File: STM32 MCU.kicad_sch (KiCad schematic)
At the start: 21 parts, among them SW3 SW_Push, SW4 SW_Push, U2 STM32G474RETx, Y1 Crystal

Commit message: Small changes
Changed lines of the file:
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@@
-		)
-	)
-	(label "FAN_PWM"
-		(at 177.8 44.45 0)
-		(effects
-			(font
-				(size 1.27 1.27)
-			)
-			(justify left bottom)
 		)
 	)
@@
 		)
 	)
+	(hierarchical_label "FAN_PWM"
+		(shape input)
+		(at 177.8 44.45 0)
+		(effects
+			(font
+				(size 1.27 1.27)
+			)
+			(justify left)
+		)
+	)

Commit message: added RTC
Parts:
- added BT1: Battery_Cell, Battery:BatteryHolder_Keystone_3000_1x12mm, symbol Device:Battery_Cell
- added U4: RV-3028-C7, Package_SON:MicroCrystal_C7_SON-8_1.5x3.2mm_P0.9mm, symbol Timer_RTC:RV-3028-C7
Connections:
- net +3V3: now also U4.7 (VDD)
- net GND: now also BT1.2 (-), U4.5 (VSS), U4.8 (EVI)
- net I2C3_SCL: now also U4.3 (SCL)
- net I2C3_SDA: now also U4.4 (SDA)
- net INT_RTC: now reaches U2.38 (PC6)
- net INT_RTC: now also U4.2 (~{INT})
- new net: BT1.1 (+), U4.6 (VBACKUP)
- no-connect marks 0 -> 1
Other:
- note added: "REAL TIME CLOCK"

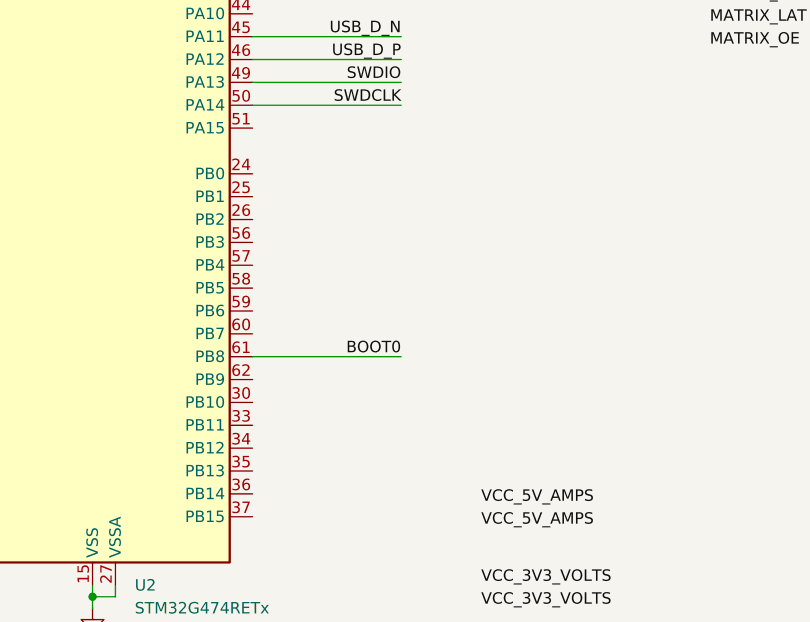
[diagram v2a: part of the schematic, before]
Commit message: added charge pump, fixed analog audio
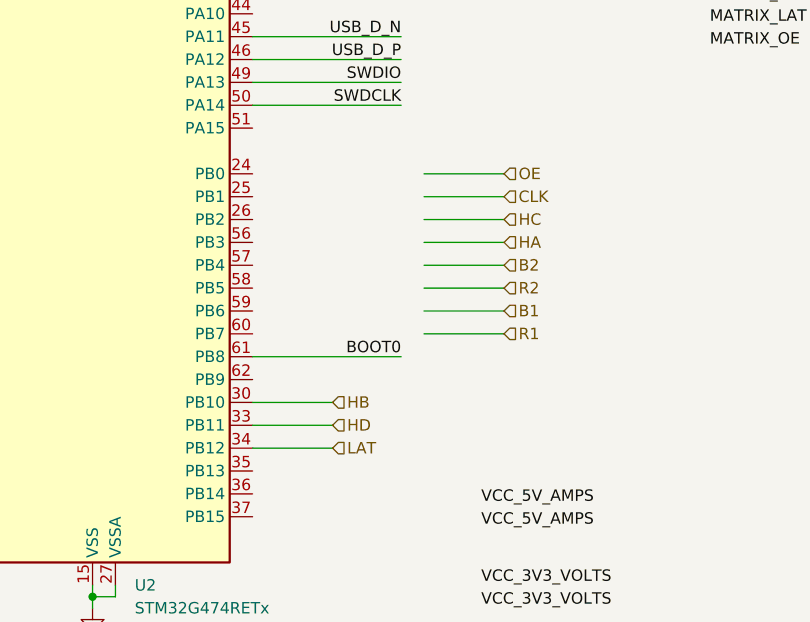
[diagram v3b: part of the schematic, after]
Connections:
- net HB: now reaches U2.30 (PB10)
- net HD: now reaches U2.33 (PB11)
- net LAT: now reaches U2.34 (PB12)
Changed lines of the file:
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@@
+	(wire
+		(pts
+			(xy 180.34 97.79) (xy 171.45 97.79)
+		)
+		(stroke
+			(width 0)
+			(type default)
+		)
+	)
 	(wire
 		(pts
@@
 	(wire
 		(pts
+			(xy 152.4 115.57) (xy 161.29 115.57)
+		)
+		(stroke
+			(width 0)
+			(type default)
+		)
+	)
+	(wire
+		(pts
 			(xy 104.14 25.4) (xy 99.06 25.4)
 		)
@@
 	(wire
 		(pts
+			(xy 152.4 120.65) (xy 161.29 120.65)
+		)
+		(stroke
+			(width 0)
+			(type default)
+		)
+	)
+	(wire
+		(pts
 			(xy 243.84 76.2) (xy 243.84 80.01)
 		)
@@
 	(wire
 		(pts
+			(xy 180.34 95.25) (xy 171.45 95.25)
+		)
+		(stroke
+			(width 0)
+			(type default)
+		)
+	)
+	(wire
+		(pts
 			(xy 152.4 110.49) (xy 168.91 110.49)
 		)
@@
 	(wire
 		(pts
+			(xy 152.4 118.11) (xy 161.29 118.11)
+		)
+		(stroke
+			(width 0)
+			(type default)
+		)
+	)
+	(wire
+		(pts
 			(xy 48.26 162.56) (xy 48.26 163.83)
 		)
@@
 	(wire
 		(pts
+			(xy 180.34 90.17) (xy 171.45 90.17)
+		)
+		(stroke
+			(width 0)
+			(type default)
+		)
+	)
+	(wire
+		(pts
 			(xy 93.98 35.56) (xy 88.9 35.56)
 		)
@@
 	(wire
 		(pts
+			(xy 180.34 100.33) (xy 171.45 100.33)
+		)
+		(stroke
+			(width 0)
+			(type default)
+		)
+	)
+	(wire
+		(pts
 			(xy 243.84 72.39) (xy 243.84 76.2)
 		)
@@
 	(wire
 		(pts
+			(xy 180.34 102.87) (xy 171.45 102.87)
+		)
+		(stroke
+			(width 0)
+			(type default)
+		)
+	)
+	(wire
+		(pts
 			(xy 260.35 115.57) (xy 264.16 115.57)
 		)
@@
 	(wire
 		(pts
+			(xy 180.34 92.71) (xy 171.45 92.71)
+		)
+		(stroke
+			(width 0)
+			(type default)
+		)
+	)
+	(wire
+		(pts
 			(xy 93.98 34.29) (xy 93.98 35.56)
 		)
@@
 	(wire
 		(pts
+			(xy 180.34 107.95) (xy 171.45 107.95)
+		)
+		(stroke
+			(width 0)
+			(type default)
+		)
+	)
+	(wire
+		(pts
 			(xy 116.84 100.33) (xy 99.06 100.33)
 		)
@@
 		(pts
 			(xy 152.4 54.61) (xy 166.37 54.61)
+		)
+		(stroke
+			(width 0)
+			(type default)
+		)
+	)
+	(wire
+		(pts
+			(xy 180.34 105.41) (xy 171.45 105.41)
 		)
 		(stroke
@@
 		)
 	)
+	(hierarchical_label "R2"
+		(shape input)
+		(at 180.34 102.87 0)
+		(effects
+			(font
+				(size 1.27 1.27)
+			)
+			(justify left)
+		)
+	)
 	(hierarchical_label "PC_7"
 		(shape input)
@@
 		)
 	)
+	(hierarchical_label "B2"
+		(shape input)
+		(at 180.34 100.33 0)
+		(effects
+			(font
+				(size 1.27 1.27)
+			)
+			(justify left)
+		)
+	)
 	(hierarchical_label "I2S3_WS"
 		(shape input)
@@
 		)
 	)
+	(hierarchical_label "OE"
+		(shape input)
+		(at 180.34 90.17 0)
+		(effects
+			(font
+				(size 1.27 1.27)
+			)
+			(justify left)
+		)
+	)
 	(hierarchical_label "ADC1_IN3"
 		(shape input)
@@
 		)
 	)
+	(hierarchical_label "CLK"
+		(shape input)
+		(at 180.34 92.71 0)
+		(effects
+			(font
+				(size 1.27 1.27)
+			)
+			(justify left)
+		)
+	)
+	(hierarchical_label "LAT"
+		(shape input)
+		(at 161.29 120.65 0)
+		(effects
+			(font
+				(size 1.27 1.27)
+			)
+			(justify left)
+		)
+	)
 	(hierarchical_label "PC_11"
 		(shape input)
@@
 		)
 	)
+	(hierarchical_label "R1"
+		(shape input)
+		(at 180.34 107.95 0)
+		(effects
+			(font
+				(size 1.27 1.27)
+			)
+			(justify left)
+		)
+	)
+	(hierarchical_label "HB"
+		(shape input)
+		(at 161.29 115.57 0)
+		(effects
+			(font
+				(size 1.27 1.27)
+			)
+			(justify left)
+		)
+	)
 	(hierarchical_label "I2S3_SD"
 		(shape input)
@@
 		)
 	)
+	(hierarchical_label "HD"
+		(shape input)
+		(at 161.29 118.11 0)
+		(effects
+			(font
+				(size 1.27 1.27)
+			)
+			(justify left)
+		)
+	)
 	(hierarchical_label "I2C3_SDA"
 		(shape input)
@@
 		)
 	)
+	(hierarchical_label "HC"
+		(shape input)
+		(at 180.34 95.25 0)
+		(effects
+			(font
+				(size 1.27 1.27)
+			)
+			(justify left)
+		)
+	)
+	(hierarchical_label "B1"
+		(shape input)
+		(at 180.34 105.41 0)
+		(effects
+			(font
+				(size 1.27 1.27)
+			)
+			(justify left)
+		)
+	)
 	(hierarchical_label "FAN_PWM"
 		(shape input)
@@
 		(effects
 			(font
+				(size 1.27 1.27)
+			)
+			(justify left)
+		)
+	)
+	(hierarchical_label "HA"
+		(shape input)
+		(at 180.34 97.79 0)
+		(effects
+			(font

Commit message: added conenctors, barreljack
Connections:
- net B1: now also U2.25 (PB1)
- net B2: now also U2.23 (PC5)
- net CLK: now also U2.20 (PA6)
- net HA: now also U2.22 (PC4)
- net HC: now also U2.21 (PA7)
- net OE: now also U2.19 (PA5)
- net R1: now also U2.26 (PB2)
- net R2: now also U2.24 (PB0)

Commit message: Minor tweaks
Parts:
- added C37, C38: C, symbol Device:C
- added Y3: Crystal, Package_QFP:LQFP-64_10x10mm_P0.5mm, symbol Device:Crystal
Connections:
- net ADC1_IN3: no longer U2.14 (PA2)
- net GND: now also C37.2, C38.2
- net I2C3_SCL: no longer U2.40 (PC8), U4.3 (SCL)
- net I2C3_SDA: no longer U2.41 (PC9), U4.4 (SDA)
- net I2S3_CK: no longer U2.52 (PC10)
- net I2S3_SD: no longer U2.54 (PC12)
- net I2S3_WS: no longer U2.18 (PA4)
- net INT_RTC: no longer U2.38 (PC6)
- net MIC: no longer U2.8 (PC0)
- net PAPIR: no longer U2.9 (PC1)
- net PC_11: no longer U2.53 (PC11)
- net PC_7: no longer U2.39 (PC7)
- net RTC_CLK_IN: now also C37.1, Y3.2
- net RTC_CLK_OUT: now also C38.1, Y3.1
- net B1: no longer names the net of U2.25 (PB1)
- net B2: no longer names the net of U2.23 (PC5)
- net CLK: no longer names the net of U2.20 (PA6)
- net HA: no longer names the net of U2.22 (PC4)
- net HB: no longer names the net of U2.30 (PB10)
- net HC: no longer names the net of U2.21 (PA7)
- net HD: no longer names the net of U2.33 (PB11)
- net LAT: no longer names the net of U2.34 (PB12)
- net OE: no longer names the net of U2.19 (PA5)
- net PA_3: no longer names the net of U2.17 (PA3)
- net R1: no longer names the net of U2.26 (PB2)
- net R2: no longer names the net of U2.24 (PB0)
- new net I2C_SCL: U4.3 (SCL)
- new net I2C_SDA: U4.4 (SDA)
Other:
- note added: "CRYSTAL RTC"

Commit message: fixing power
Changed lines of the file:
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@@
+		)
+	)
+	(hierarchical_label "LED_On"
+		(shape input)
+		(at 85.09 130.81 180)
+		(effects
+			(font
+				(size 1.27 1.27)
+			)
+			(justify right)
 		)
 	)

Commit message: Wednesday minor changes
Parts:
- added D6, D9: LED, symbol Device:LED
- added R36, R48: 330, Package_DIP:DIP-8_W7.62mm, symbol Device:R
- added R46, R47: 5k1, Package_DIP:DIP-8_W7.62mm, symbol Device:R
- added R55: 10k, Package_DIP:DIP-8_W7.62mm, symbol Device:R
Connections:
- net I2C_SCL is gone; now on net I2C3_SCL: U4.3 (SCL)
- net I2C_SDA is gone; now on net I2C3_SDA: U4.4 (SDA)
- net +3V3: now also R36.1, R46.2, R47.2, R55.1
- net 5V_VOLTS: now also U2.17 (PA3)
- net ALS_ADC: now also U2.12 (PA0)
- net EXT_TEMP: now also U2.14 (PA2)
- net FAN_PWM: now also U2.9 (PC1)
- net GND: now also D6.1 (K), D9.1 (K)
- net I2C3_SCL: now also U2.42 (PA8), R46.1
- net I2C3_SDA: now also U2.41 (PC9), R47.1
- net MIC_ADC: now also U2.13 (PA1)
- net TV_IR_PWM: now also U2.8 (PC0)
- net at U2.18 (PA4): now also R55.2
- new net: D9.2 (A), R48.2
- new net: D6.2 (A), R36.2
- new net TEST_LED: R48.1
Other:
- note added: "I2C PULLUPS"
- note added: "TEST LED"
- moved on the sheet: C11, C3, C37, C38, R3, R4, Y1, Y3

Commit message: hooking stuff up to STM
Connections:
- net I2C3_SDA: now also U2.53 (PC11); no longer U2.41 (PC9)
- net I2S3_CK: now also U2.35 (PB13)
- net I2S3_SD: now also U2.37 (PB15)
- net I2S3_WS: now also U2.34 (PB12)
- net SPI_CS_ESP: now also U2.22 (PC4)
- net SPI_MISO: now also U2.20 (PA6)
- net SPI_MOSI: now also U2.21 (PA7)
- net SPI_SCLK: now also U2.19 (PA5)
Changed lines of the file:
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@@
 			(width 0)
 			(type default)
+			(color 0 194 194 1)
 		)
 	)
@@
 			(width 0)
 			(type default)
+			(color 0 194 194 1)
 		)
 	)
@@
 	(wire
 		(pts
+			(xy 185.42 119.38) (xy 189.23 119.38)
+		)
+		(stroke
+			(width 0)
+			(type default)
+			(color 0 0 194 1)
+		)
+	)
+	(wire
+		(pts
 			(xy 125.73 162.56) (xy 125.73 163.83)
 		)
@@
 	(wire
 		(pts
+			(xy 152.4 128.27) (xy 166.37 128.27)
+		)
+		(stroke
+			(width 0)
+			(type default)
+			(color 194 0 194 1)
+		)
+	)
+	(wire
+		(pts
 			(xy 40.64 93.98) (xy 40.64 96.52)
 		)
@@
 	(wire
 		(pts
+			(xy 152.4 123.19) (xy 166.37 123.19)
+		)
+		(stroke
+			(width 0)
+			(type default)
+			(color 194 0 194 1)
+		)
+	)
+	(wire
+		(pts
 			(xy 152.4 54.61) (xy 156.21 54.61)
 		)
@@
 	(wire
 		(pts
+			(xy 185.42 127) (xy 189.23 127)
+		)
+		(stroke
+			(width 0)
+			(type default)
+			(color 0 0 194 1)
+		)
+	)
+	(wire
+		(pts
 			(xy 80.01 25.4) (xy 80.01 26.67)
 		)
@@
 	(wire
 		(pts
+			(xy 152.4 64.77) (xy 177.8 64.77)
+		)
+		(stroke
+			(width 0)
+			(type default)
+			(color 221 133 0 1)
+		)
+	)
+	(wire
+		(pts
 			(xy 35.56 96.52) (xy 40.64 96.52)
 		)
@@
 	(wire
 		(pts
+			(xy 152.4 120.65) (xy 166.37 120.65)
+		)
+		(stroke
+			(width 0)
+			(type default)
+			(color 194 0 194 1)
+		)
+	)
+	(wire
+		(pts
 			(xy 243.84 76.2) (xy 243.84 80.01)
 		)
@@
 	(wire
 		(pts
+			(xy 185.42 124.46) (xy 189.23 124.46)
+		)
+		(stroke
+			(width 0)
+			(type default)
+			(color 0 0 194 1)
+		)
+	)
+	(wire
+		(pts
 			(xy 88.9 35.56) (xy 80.01 35.56)
 		)
@@
 	(wire
 		(pts
+			(xy 105.41 80.01) (xy 116.84 80.01)
+		)
+		(stroke
+			(width 0)
+			(type default)
+			(color 221 133 0 1)
+		)
+	)
+	(wire
+		(pts
 			(xy 85.09 171.45) (xy 85.09 180.34)
 		)
@@
 	(wire
 		(pts
+			(xy 185.42 121.92) (xy 189.23 121.92)
+		)
+		(stroke
+			(width 0)
+			(type default)
+			(color 0 0 194 1)
+		)
+	)
+	(wire
+		(pts
 			(xy 99.06 52.07) (xy 116.84 52.07)
 		)
@@
 	(wire
 		(pts
+			(xy 185.42 129.54) (xy 189.23 129.54)
+		)
+		(stroke
+			(width 0)
+			(type default)
+			(color 0 0 194 1)
+		)
+	)
+	(wire
+		(pts
 			(xy 134.62 137.16) (xy 137.16 137.16)
 		)
@@
 	(wire
 		(pts
+			(xy 109.22 97.79) (xy 116.84 97.79)
+		)
+		(stroke
+			(width 0)
+			(type default)
+		)
+	)
+	(wire
+		(pts
 			(xy 30.48 82.55) (xy 30.48 86.36)
 		)
@@
 	(wire
 		(pts
+			(xy 152.4 59.69) (xy 177.8 59.69)
+		)
+		(stroke
+			(width 0)
+			(type default)
+			(color 221 133 0 1)
+		)
+	)
+	(wire
+		(pts
 			(xy 35.56 59.69) (xy 30.48 59.69)
 		)
@@
 	(wire
 		(pts
-			(xy 111.76 92.71) (xy 116.84 92.71)
-		)
-		(stroke
-			(width 0)
-			(type default)
-		)
-	)
-	(wire
-		(pts
 			(xy 278.13 80.01) (xy 278.13 76.2)
 		)
@@
 			(width 0)
 			(type default)
+		)
+	)
+	(wire
+		(pts
+			(xy 152.4 62.23) (xy 177.8 62.23)
+		)
+		(stroke
+			(width 0)
+			(type default)
+			(color 221 133 0 1)
 		)
 	)
@@
 	(hierarchical_label "SPI_SCLK"
 		(shape input)
-		(at 190.5 49.53 0)
+		(at 177.8 59.69 0)
 		(effects
 			(font
@@
 	(hierarchical_label "SPI_MISO"
 		(shape input)
-		(at 190.5 46.99 0)
+		(at 177.8 62.23 0)
 		(effects
 			(font
@@
 	(hierarchical_label "I2S3_WS"
 		(shape input)
-		(at 205.74 104.14 0)
+		(at 166.37 120.65 0)
 		(effects
 			(font
@@
 	(hierarchical_label "I2C3_SDA"
 		(shape input)
-		(at 111.76 92.71 180)
+		(at 109.22 97.79 180)
 		(effects
 			(font
@@
 		)
 	)
-	(hierarchical_label "SPEAKER"
-		(shape input)
-		(at 190.5 31.75 0)
-		(effects
-			(font
-				(size 1.27 1.27)
-			)
-			(justify left)
-		)
-	)
 	(hierarchical_label "3V3_VOLTS"
 		(shape input)
@@
 	(hierarchical_label "MATRIX_G1"
 		(shape input)
-		(at 176.53 123.19 0)
+		(at 189.23 119.38 0)
 		(effects
 			(font
@@
 	(hierarchical_label "ADC1_IN3"
 		(shape input)
-		(at 177.8 59.69 0)
+		(at 177.8 72.39 0)
 		(effects
 			(font
@@
 	(hierarchical_label "MATRIX_B"
 		(shape input)
-		(at 176.53 128.27 0)
+		(at 189.23 124.46 0)
 		(effects
 			(font
@@
 	(hierarchical_label "I2S3_SD"
 		(shape input)
-		(at 210.82 110.49 180)
+		(at 166.37 128.27 0)
+		(effects
+			(font
+				(size 1.27 1.27)
+			)
+			(justify left)
+		)
+	)
+	(hierarchical_label "MIC_ADC"
+		(shape input)
+		(at 156.21 49.53 0)
+		(effects
+			(font
+				(size 1.27 1.27)
+			)
+			(justify left)
+		)
+	)
+	(hierarchical_label "MATRIX_D"
+		(shape input)
+		(at 189.23 127 0)
+		(effects
+			(font
+				(size 1.27 1.27)
+			)
+			(justify left)
+		)
+	)
+	(hierarchical_label "MATRIX_LAT"
+		(shape input)
+		(at 189.23 129.54 0)
+		(effects
+			(font
+				(size 1.27 1.27)
+			)
+			(justify left)
+		)
+	)
+	(hierarchical_label "MATRIX_R1"
+		(shape input)
+		(at 176.53 138.43 0)
+		(effects
+			(font
+				(size 1.27 1.27)
+			)
+			(justify left)
+		)
+	)
+	(hierarchical_label "SPI_MOSI"
+		(shape input)
+		(at 177.8 64.77 0)
+		(effects
+			(font
+				(size 1.27 1.27)
+			)
+			(justify left)
+		)
+	)
+	(hierarchical_label "SPI_CS_ESP"
+		(shape input)
+		(at 105.41 80.01 180)
 		(effects
 			(font
@@
 		)
 	)
-	(hierarchical_label "MIC_ADC"
-		(shape input)
-		(at 156.21 49.53 0)
-		(effects
-			(font
-				(size 1.27 1.27)
-			)
-			(justify left)
-		)
-	)
-	(hierarchical_label "MATRIX_D"
-		(shape input)
-		(at 176.53 130.81 0)
-		(effects
-			(font
-				(size 1.27 1.27)
-			)
-			(justify left)
-		)
-	)
-	(hierarchical_label "MATRIX_LAT"
-		(shape input)
-		(at 176.53 133.35 0)
-		(effects
-			(font
-				(size 1.27 1.27)
-			)
-			(justify left)
-		)
-	)
-	(hierarchical_label "MATRIX_R1"
-		(shape input)
-		(at 176.53 138.43 0)
-		(effects
-			(font
-				(size 1.27 1.27)
-			)
-			(justify left)
-		)
-	)
-	(hierarchical_label "SPI_MOSI"
-		(shape input)
-		(at 190.5 44.45 0)
-		(effects
-			(font
-				(size 1.27 1.27)
-			)
-			(justify left)
-		)
-	)
-	(hierarchical_label "SPI_CS_ESP"
-		(shape input)
-		(at 190.5 52.07 0)
-		(effects
-			(font
-				(size 1.27 1.27)
-			)
-			(justify left)
-		)
-	)
 	(hierarchical_label "I2C3_SCL"
 		(shape input)
@@
 	(hierarchical_label "MATRIX_G2"
 		(shape input)
-		(at 176.53 125.73 0)
+		(at 189.23 121.92 0)
 		(effects
 			(font
@@
 	(hierarchical_label "I2S3_CK"
 		(shape input)
-		(at 210.82 107.95 180)
-		(effects
-			(font
-				(size 1.27 1.27)
-			)
-			(justify right)
-		)
-	)
+		(at 166.37 123.19 0)
+		(effects
+			(font
+				(size 1.27 1.27)
+			)
+			(justify left)
+		)
+	)
